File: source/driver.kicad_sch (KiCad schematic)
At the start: 50 parts

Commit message: Add files via upload
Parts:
- gave numbers to parts that had none: 50
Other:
- moved on the sheet: D9

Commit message: Changes suggested by mxlemming, Elwin and hackey on Discord
New power supplies and using other op-amps for current sense
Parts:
- removed C13, C28: 100u, symbol Device:C_Polarized_US
- removed C14, C19: 2.2u, symbol Device:C
- removed C17: 15n, symbol Device:C
- removed C22: 47u @ 100V, symbol Device:C_Polarized_US
- removed C23: 1u @ 100V, symbol Device:C
- removed C26: 47p, symbol Device:C
- removed C27: 22u, symbol Device:C
- removed D8: D_Schottky, symbol Device:D_Schottky
- removed IC1: BD9G101G-TR, Custom:SSOP6, symbol Custom_Library:BD9G101G-TR
- removed L2: 68uH, symbol pspice:INDUCTOR
- removed U7: HT1015AREZ, Custom:HT1015AREZ_SOIC8E, symbol Custom_Library:HT1015AREZ
- added C13, C14: 2.2u, Capacitor_SMD:C_0603_1608Metric, symbol BLDC_4-rescue:C-RESCUE-BLDC_4
- added C17, C26: 100u, symbol Device:C_Polarized_US
- added C19: 47u @ 100v, symbol Device:C_Polarized_US
- added C22, C23: 4.7u, Capacitor_SMD:C_0603_1608Metric, symbol BLDC_4-rescue:C-RESCUE-BLDC_4
- added D24: D_Schottky, symbol Device:D_Schottky
- added D8: 1N4148W, Diode_SMD:D_SOD-123, symbol Diode:1N4148W
- added R28: 1k8, symbol Device:R
- added R33: 0.06R, symbol Device:R
- added R34: 3k, symbol Device:R
- added U7: AMS1117-5.0, Package_TO_SOT_SMD:SOT-223-3_TabPin2, symbol Regulator_Linear:AMS1117-5.0
- added U8: TX4130L/PW2902, symbol Custom_Library:TX4130L / PW2902
- C15: value 100n -> 2.2u
- C20: value 2.2u -> 1u @ 100V
- C25: value 100n -> 22u
- L1: value 6.8uH -> 68uH
- R18: value 3k9 -> 82k
- R19: value 680R -> 1k8
- R24: value 10k -> 56k
- R25: value 560R -> 56k
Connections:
- net +5V: now also C17.1, U7.2 (VO); no longer C7.2, C9.2, L1.2, R18.1, U3.3 (VI)
- net GND: now also C15.2, C20.2, C25.2, R25.1, C13.1, C14.1, C17.2, C19.2, C26.2, D24.2 (A), R34.1, U7.1 (GND); no longer C20.1, D11.2 (A), R19.2, R25.2
- net V_IN: now also C20.1, R18.2, C19.1, U8.1 (VIN), U8.9 (VIN)
- net at L1.1: now also D11.2 (A), R19.1, C22.1, C23.1, R28.1, R33.1, U8.6 (VSS)
- net at R24.2: now also R19.2, U8.3 (FB1); no longer R25.1
- net at D11.1 (K): now also R18.1, C22.2, D8.1 (K), U8.2 (VDD); no longer C25.2
- net +12V: now reaches C25.1
- net +12V: now also C16.1, C21.1, C7.2, C8.1, C9.2, D4.2 (A), D6.2 (A), D9.2 (A), L1.2, R24.1, U3.3 (VI), U4.1 (VCC), U5.1 (VCC), U6.1 (VCC), C13.2, C14.2, C26.1, D8.2 (A), R34.2, U7.3 (VI)
- removed net +15V: C16.1, C20.2, C21.1, C8.1, D4.2 (A), D6.2 (A), D9.2 (A), R24.1, U4.1 (VCC), U5.1 (VCC), U6.1 (VCC)
- new net: D24.1 (K), R33.2, U8.7 (VSEN), U8.8 (VSEND)
- new net: R25.2, R28.2, U8.4 (FB2)
- new net: C23.2, U8.5 (LDO)
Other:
- note added: "F-Of-C"
- note added: "TX4130L"
- note added: "TX4130L: VFB: min=369 typ=380 max=391 mV VCS: min=145 typ=150 max=155 mV R1 = R3 R2 = R4 Vout= VFB * (R2+R1)/R1 Iout=VCS/R7 (R7=0.06R -> Io=2.6A) Frequency: Fixed 140kHz Inductance: 33uH-100uH"
- note added: "https://datasheet.lcsc.com/lcsc/1912231403_XDS-TX4130L_C448635.pdf https://www.pwchip.com/en/product/PW2902-174.html"
- note removed: "Free-Of-Charge"
- note removed: "In order to minimize losses associated with the reverse recovery properties of the diode and ground noise bouncing, a fast recovery diode or Schottky diode with low forward voltage drop and low junction capacitance is recommended. Using Schottky diodes reduce the risk associated with charge supplied back to the gate driver supply from the bootstrap capacitor and minimize leakage current."
- moved on the sheet: R26, R27

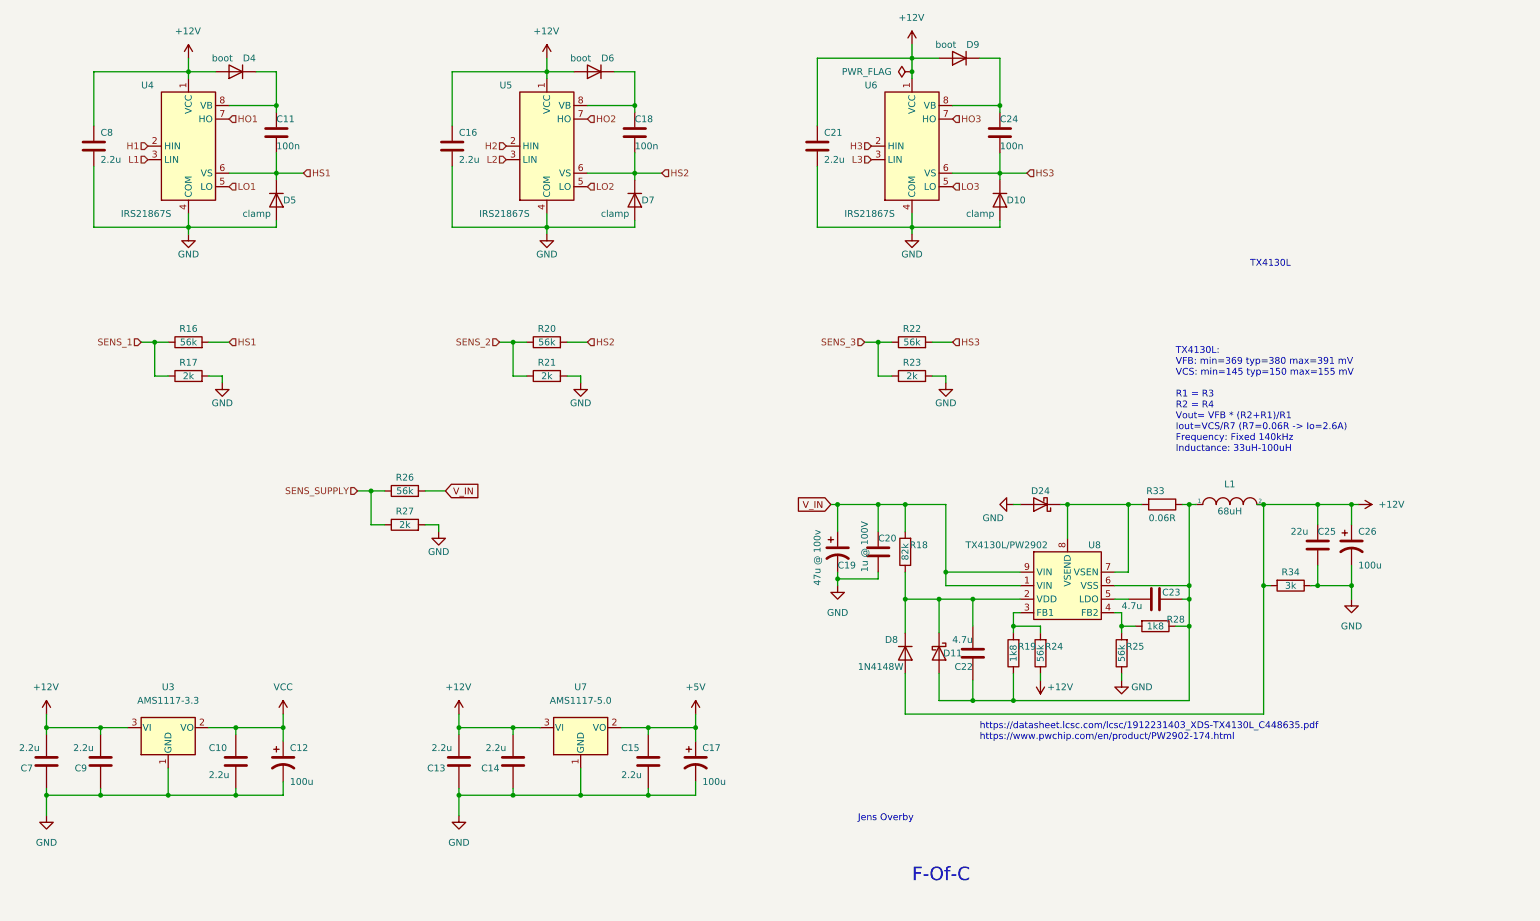
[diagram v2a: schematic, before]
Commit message: First attempt of layout
It's a rats nest. Will have to remove some connections temporarily for the first prototype.
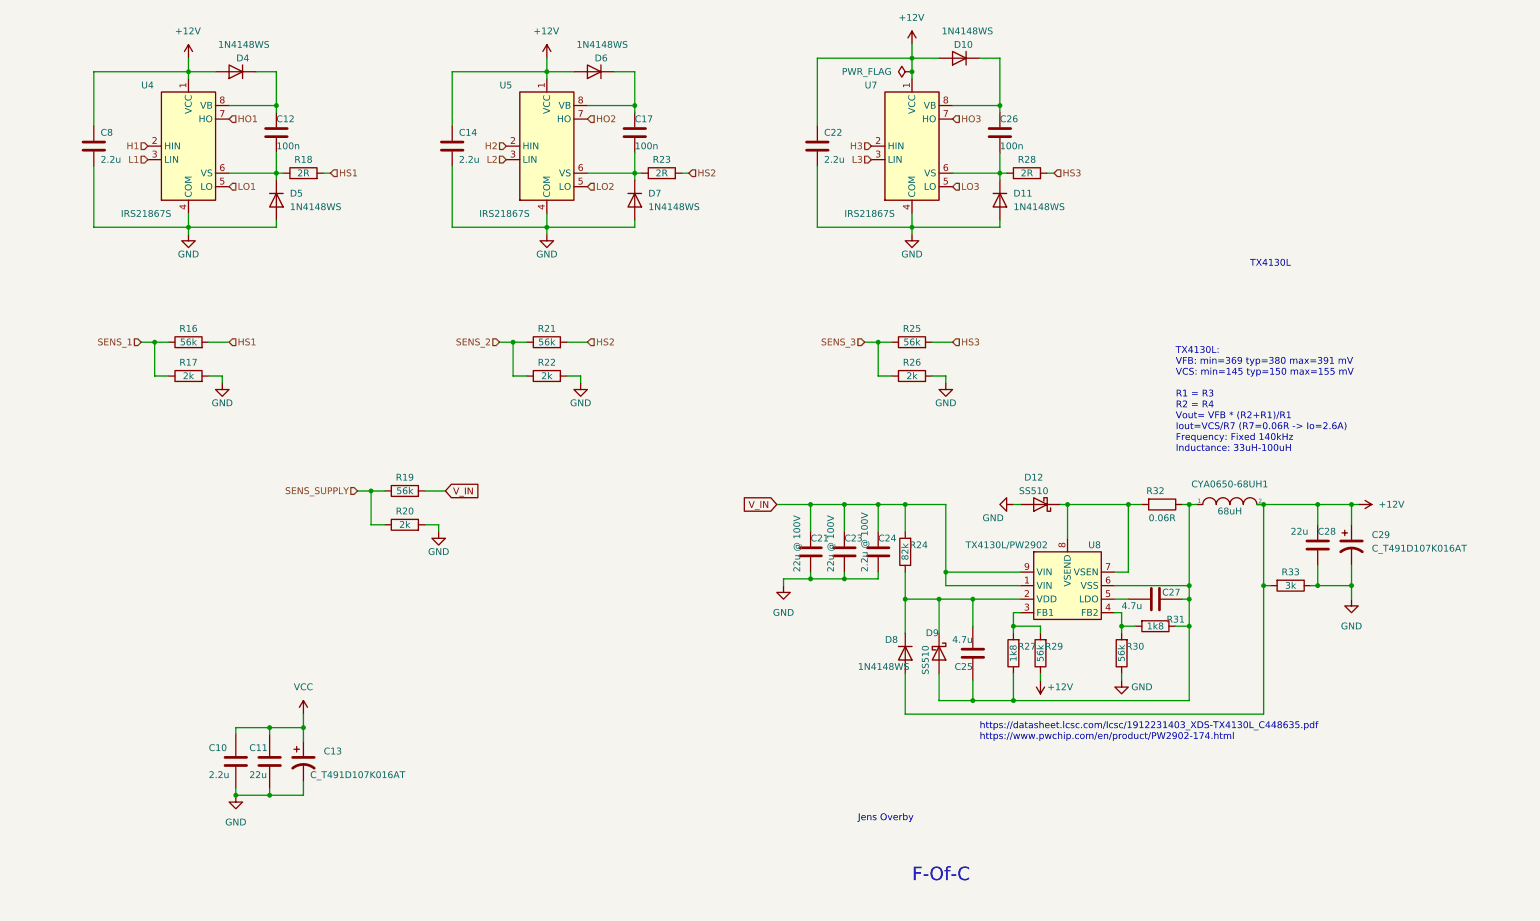
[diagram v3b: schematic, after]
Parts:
- removed C12, C17, C26: 100u, symbol Device:C_Polarized_US
- removed C13, C14, C15, C7, C9: 2.2u, Capacitor_SMD:C_0603_1608Metric, symbol BLDC_4-rescue:C-RESCUE-BLDC_4
- removed C19: 47u @ 100v, symbol Device:C_Polarized_US
- removed D10, D5, D7: clamp, symbol Device:D
- removed D11: D_Schottky, symbol Device:D_Schottky
- removed D4, D6, D9: boot, symbol Device:D
- removed U3: AMS1117-3.3, Package_TO_SOT_SMD:SOT-223-3_TabPin2, symbol Regulator_Linear:AMS1117-3.3
- removed U7: AMS1117-5.0, Package_TO_SOT_SMD:SOT-223-3_TabPin2, symbol Regulator_Linear:AMS1117-5.0
- added C11: 22u, Capacitor_SMD:C_0603_1608Metric, symbol BLDC_4-rescue:C-RESCUE-BLDC_4
- added C13, C29: C_T491D107K016AT, Custom:T491D107K016AT_cap, symbol Custom_Library:C_T491D107K016AT
- added C21, C23: 22u @ 100V, Capacitor_SMD:C_0603_1608Metric, symbol Device:C
- added D10, D11, D4, D5, D6, D7: 1N4148WS, Diode_SMD:D_SOD-323, symbol Diode:1N4148W
- added D9: SS510, Diode_SMD:D_1206_3216Metric, symbol Device:D_Schottky
- added R18, R23, R28: 2R, Resistor_SMD:R_0402_1005Metric, symbol Device:R
- C12: renamed from C11; footprint (none) -> Capacitor_SMD:C_0603_1608Metric
- C14: renamed from C16; footprint (none) -> Capacitor_SMD:C_0603_1608Metric
- C17: renamed from C18; footprint (none) -> Capacitor_SMD:C_0603_1608Metric
- C22: renamed from C21; footprint (none) -> Capacitor_SMD:C_0603_1608Metric
- C24: renamed from C20; value 1u @ 100V -> 2.2u @ 100V; footprint (none) -> Capacitor_SMD:C_0603_1608Metric
- C26: renamed from C24; footprint (none) -> Capacitor_SMD:C_0603_1608Metric
- C28: renamed from C25; footprint (none) -> Capacitor_SMD:C_0603_1608Metric
- C8: footprint (none) -> Capacitor_SMD:C_0603_1608Metric
- CYA0650-68UH1: renamed from L1; footprint (none) -> Custom:L_6.6x7.2_H5.0_CYA0650_68UH
- D12: renamed from D24; value D_Schottky -> SS510; footprint (none) -> Diode_SMD:D_1206_3216Metric
- D8: value 1N4148W -> 1N4148WS; footprint Diode_SMD:D_SOD-123 -> Diode_SMD:D_SOD-323
- R16, R17: footprint (none) -> Resistor_SMD:R_0402_1005Metric
- R19: renamed from R26; footprint (none) -> Resistor_SMD:R_0402_1005Metric
- R20: renamed from R27; footprint (none) -> Resistor_SMD:R_0402_1005Metric
- R21: renamed from R20; footprint (none) -> Resistor_SMD:R_0402_1005Metric
- R22: renamed from R21; footprint (none) -> Resistor_SMD:R_0402_1005Metric
- R24: renamed from R18; footprint (none) -> Resistor_SMD:R_0402_1005Metric
- R25: renamed from R22; footprint (none) -> Resistor_SMD:R_0402_1005Metric
- R26: renamed from R23; footprint (none) -> Resistor_SMD:R_0402_1005Metric
- R27: renamed from R19; footprint (none) -> Resistor_SMD:R_0402_1005Metric
- R29: renamed from R24; footprint (none) -> Resistor_SMD:R_0402_1005Metric
- R30: renamed from R25; footprint (none) -> Resistor_SMD:R_0402_1005Metric
- R31: renamed from R28; footprint (none) -> Resistor_SMD:R_0402_1005Metric
- R32: renamed from R33; footprint (none) -> Resistor_SMD:R_0402_1005Metric
- R33: renamed from R34; footprint (none) -> Resistor_SMD:R_0402_1005Metric
- U8: footprint (none) -> Custom:TX4130L_ESOP-8
- renumbered C22 to C25, C23 to C27, U6 to U7
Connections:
- net +12V: now also C29.1, D10.2 (A), D4.2 (A), D6.2 (A)
- net GND: now also C11.2, C13.2, C21.2, C23.2, C29.2, D11.2 (A), D5.2 (A), D7.2 (A)
- net HS1: now also R18.2; no longer C12.2, U4.6 (VS)
- net HS2: now also R23.2; no longer C17.2, U5.6 (VS)
- net HS3: now also R28.2; no longer C26.2, U7.6 (VS)
- net VCC: now also C11.1, C13.1
- net V_IN: now also C21.1, C23.1
- net at C25.2, D8.1 (K), R24.1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: now also D9.1 (K)
- net at C25.1, C27.1, CYA0650-68UH1.1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: now also D9.2 (A)
- net at C26.1, U7.8 (VB): now also D10.1 (K)
- net at C12.1, U4.8 (VB): now also D4.1 (K)
- net at C17.1, U5.8 (VB): now also D6.1 (K)
- new net: C12.2, D5.1 (K), R18.1, U4.6 (VS)
- new net: C26.2, D11.1 (K), R28.1, U7.6 (VS)
- new net: C17.2, D7.1 (K), R23.1, U5.6 (VS)

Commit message: Most components now jlcpcb basic
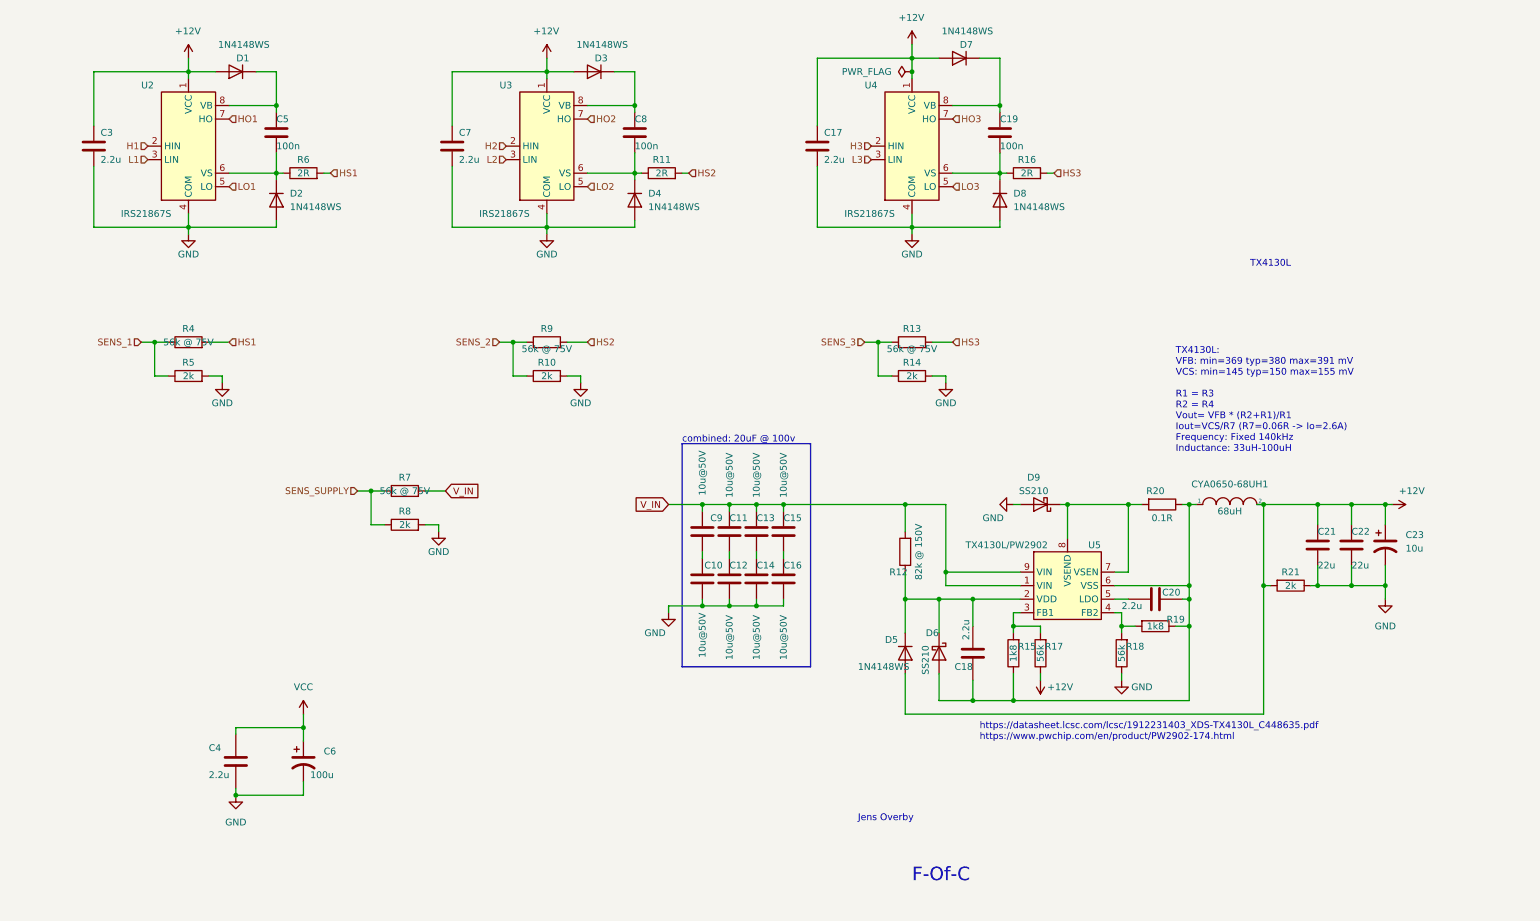
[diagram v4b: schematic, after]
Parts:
- removed C11: 22u, Capacitor_SMD:C_0603_1608Metric, symbol BLDC_4-rescue:C-RESCUE-BLDC_4
- removed C24: 2.2u @ 100V, Capacitor_SMD:C_0603_1608Metric, symbol Device:C
- added C10, C12, C14, C15, C16, C9: 10u@50V, Capacitor_SMD:C_1206_3216Metric, symbol Device:C
- added C22: 22u, Capacitor_SMD:C_0805_2012Metric, symbol Device:C
- C11: renamed from C21; value 22u @ 100V -> 10u@50V; footprint Capacitor_SMD:C_0603_1608Metric -> Capacitor_SMD:C_1206_3216Metric; LCSC (none) -> C13585
- C13: renamed from C23; value 22u @ 100V -> 10u@50V; footprint Capacitor_SMD:C_0603_1608Metric -> Capacitor_SMD:C_1206_3216Metric; LCSC (none) -> C13585
- C17: renamed from C22; LCSC (none) -> C23630
- C18: renamed from C25; value 4.7u -> 2.2u; LCSC (none) -> C23630
- C19: renamed from C26; footprint Capacitor_SMD:C_0603_1608Metric -> Capacitor_SMD:C_0402_1005Metric; LCSC (none) -> C1525
- C20: renamed from C27; value 4.7u -> 2.2u; LCSC (none) -> C23630
- C21: renamed from C28; footprint Capacitor_SMD:C_0603_1608Metric -> Capacitor_SMD:C_0805_2012Metric; LCSC (none) -> C45783
- C23: renamed from C29; value C_T491D107K016AT -> 10u; footprint Custom:T491D107K016AT_cap -> Capacitor_Tantalum_SMD:CP_EIA-3216-10_Kemet-I; LCSC (none) -> C7171
- C3: renamed from C8; LCSC (none) -> C23630
- C4: renamed from C10; LCSC (none) -> C23630
- C5: renamed from C12; footprint Capacitor_SMD:C_0603_1608Metric -> Capacitor_SMD:C_0402_1005Metric; LCSC (none) -> C1525
- C6: renamed from C13; value C_T491D107K016AT -> 100u; footprint Custom:T491D107K016AT_cap -> Capacitor_Tantalum_SMD:CP_EIA-3528-21_Kemet-B; LCSC (none) -> C16133
- C7: renamed from C14; LCSC (none) -> C23630
- C8: renamed from C17; footprint Capacitor_SMD:C_0603_1608Metric -> Capacitor_SMD:C_0402_1005Metric; LCSC (none) -> C1525
- CYA0650-68UH1: LCSC (none) -> C5189964
- D1: renamed from D4; LCSC (none) -> C2128
- D2: renamed from D5; LCSC (none) -> C2128
- D3: renamed from D6; LCSC (none) -> C2128
- D4: renamed from D7; LCSC (none) -> C2128
- D5: renamed from D8; LCSC (none) -> C2128
- D6: renamed from D9; value SS510 -> SS210; footprint Diode_SMD:D_1206_3216Metric -> Diode_SMD:D_SMA; LCSC (none) -> C14996
- D7: renamed from D10; LCSC (none) -> C2128
- D8: renamed from D11; LCSC (none) -> C2128
- D9: renamed from D12; value SS510 -> SS210; footprint Diode_SMD:D_1206_3216Metric -> Diode_SMD:D_SMA; LCSC (none) -> C14996
- R10: renamed from R22; LCSC (none) -> C4109
- R11: renamed from R23; footprint Resistor_SMD:R_0402_1005Metric -> Resistor_SMD:R_0603_1608Metric; LCSC (none) -> C22977
- R12: renamed from R24; value 82k -> 82k @ 150V; footprint Resistor_SMD:R_0402_1005Metric -> Resistor_SMD:R_0805_2012Metric; LCSC (none) -> C17840
- R13: renamed from R25; value 56k -> 56k @ 75V; footprint Resistor_SMD:R_0402_1005Metric -> Resistor_SMD:R_0603_1608Metric; LCSC (none) -> C23206
- R14: renamed from R26; LCSC (none) -> C4109
- R15: renamed from R27; footprint Resistor_SMD:R_0402_1005Metric -> Resistor_SMD:R_0603_1608Metric; LCSC (none) -> C4177
- R16: renamed from R28; footprint Resistor_SMD:R_0402_1005Metric -> Resistor_SMD:R_0603_1608Metric; LCSC (none) -> C22977
- R17: renamed from R29; footprint Resistor_SMD:R_0402_1005Metric -> Resistor_SMD:R_0603_1608Metric; LCSC (none) -> C23206
- R18: renamed from R30; footprint Resistor_SMD:R_0402_1005Metric -> Resistor_SMD:R_0603_1608Metric; LCSC (none) -> C23206
- R19: renamed from R31; footprint Resistor_SMD:R_0402_1005Metric -> Resistor_SMD:R_0603_1608Metric; LCSC (none) -> C4177
- R20: renamed from R32; value 0.06R -> 0.1R; footprint Resistor_SMD:R_0402_1005Metric -> Resistor_SMD:R_1206_3216Metric; LCSC (none) -> C25334
- R21: renamed from R33; value 3k -> 2k; LCSC (none) -> C4109
- R4: renamed from R16; value 56k -> 56k @ 75V; footprint Resistor_SMD:R_0402_1005Metric -> Resistor_SMD:R_0603_1608Metric; LCSC (none) -> C23206
- R5: renamed from R17; LCSC (none) -> C4109
- R6: renamed from R18; footprint Resistor_SMD:R_0402_1005Metric -> Resistor_SMD:R_0603_1608Metric; LCSC (none) -> C22977
- R7: renamed from R19; value 56k -> 56k @ 75V; footprint Resistor_SMD:R_0402_1005Metric -> Resistor_SMD:R_0603_1608Metric; LCSC (none) -> C23206
- R8: renamed from R20; LCSC (none) -> C4109
- R9: renamed from R21; value 56k -> 56k @ 75V; footprint Resistor_SMD:R_0402_1005Metric -> Resistor_SMD:R_0603_1608Metric; LCSC (none) -> C23206
- U2: renamed from U4; LCSC (none) -> C52290
- U3: renamed from U5; LCSC (none) -> C52290
- U4: renamed from U7; LCSC (none) -> C52290
- U5: renamed from U8; LCSC (none) -> C448635
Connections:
- net +12V: now also C22.1
- net GND: now also C10.1, C12.2, C14.2, C16.2, C22.2; no longer C11.2, C13.2
- net V_IN: now also C15.1, C9.2
- new net: C15.2, C16.1
- new net: C13.2, C14.1
- new net: C11.2, C12.1
- new net: C10.2, C9.1
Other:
- note added: "combined: 20uF @ 100v"
- moved on the sheet: C11, C13, C23

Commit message: Add files via upload
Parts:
- removed C13, C14, C15, C16: 10u@50V, Capacitor_SMD:C_1206_3216Metric, symbol Device:C
- C19, C5, C8: footprint Capacitor_SMD:C_0402_1005Metric -> Capacitor_SMD:C_0603_1608Metric; LCSC C1525 -> C14663
- R13: renamed from R14; footprint Resistor_SMD:R_0402_1005Metric -> Resistor_SMD:R_0603_1608Metric; LCSC C4109 -> C22975
- R20: renamed from R21; footprint Resistor_SMD:R_0402_1005Metric -> Resistor_SMD:R_0603_1608Metric; LCSC C4109 -> C22975
- R4: renamed from R5; footprint Resistor_SMD:R_0402_1005Metric -> Resistor_SMD:R_0603_1608Metric; LCSC C4109 -> C22975
- R7: renamed from R8; footprint Resistor_SMD:R_0402_1005Metric -> Resistor_SMD:R_0603_1608Metric; LCSC C4109 -> C22975
- R9: renamed from R10; footprint Resistor_SMD:R_0402_1005Metric -> Resistor_SMD:R_0603_1608Metric; LCSC C4109 -> C22975
- renumbered R11 to R10, R12 to R11, R13 to R12, R15 to R14, R16 to R15, R17 to R16, R18 to R17, R19 to R18, R20 to R19, R4 to R3, R6 to R5, R7 to R6, R9 to R8
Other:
- moved on the sheet: C10, C11, C12, C9
